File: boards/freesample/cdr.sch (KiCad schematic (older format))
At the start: 75 parts, among them J6 XILINX_JTAG, U13 SIP32408, U5 TLK10232, U6 LMK61PD0A2

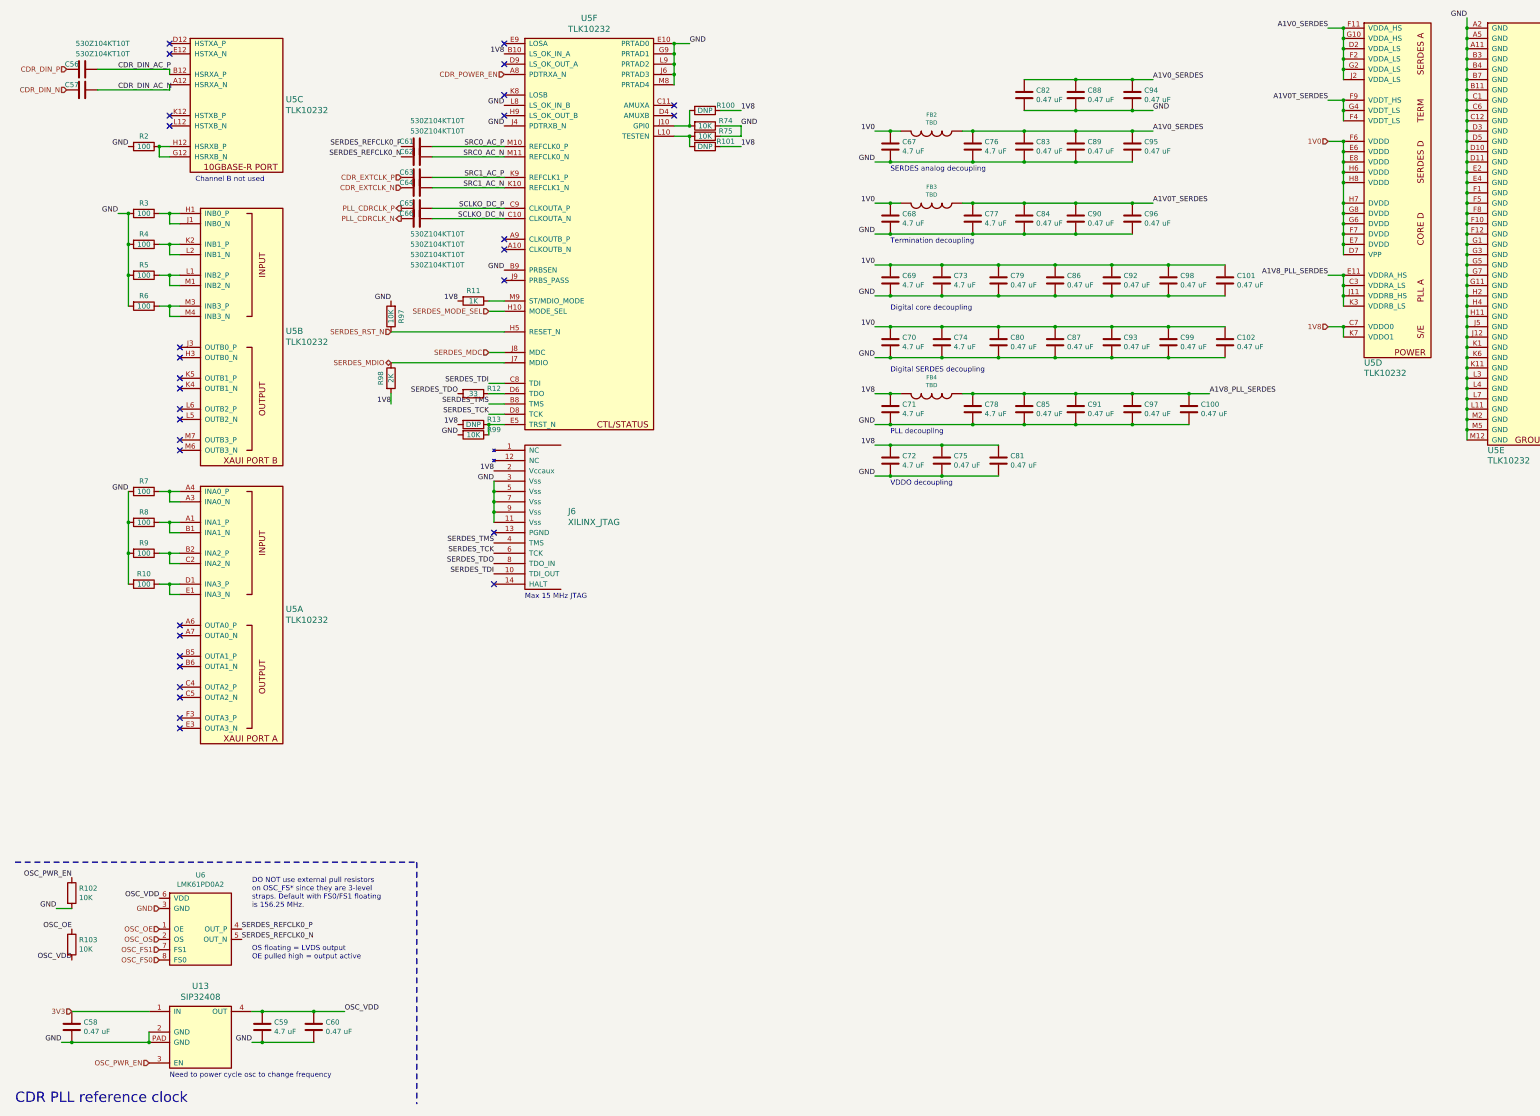
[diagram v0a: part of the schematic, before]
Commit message: Added more test points. Started picking packages for passives. Continued schematic review.
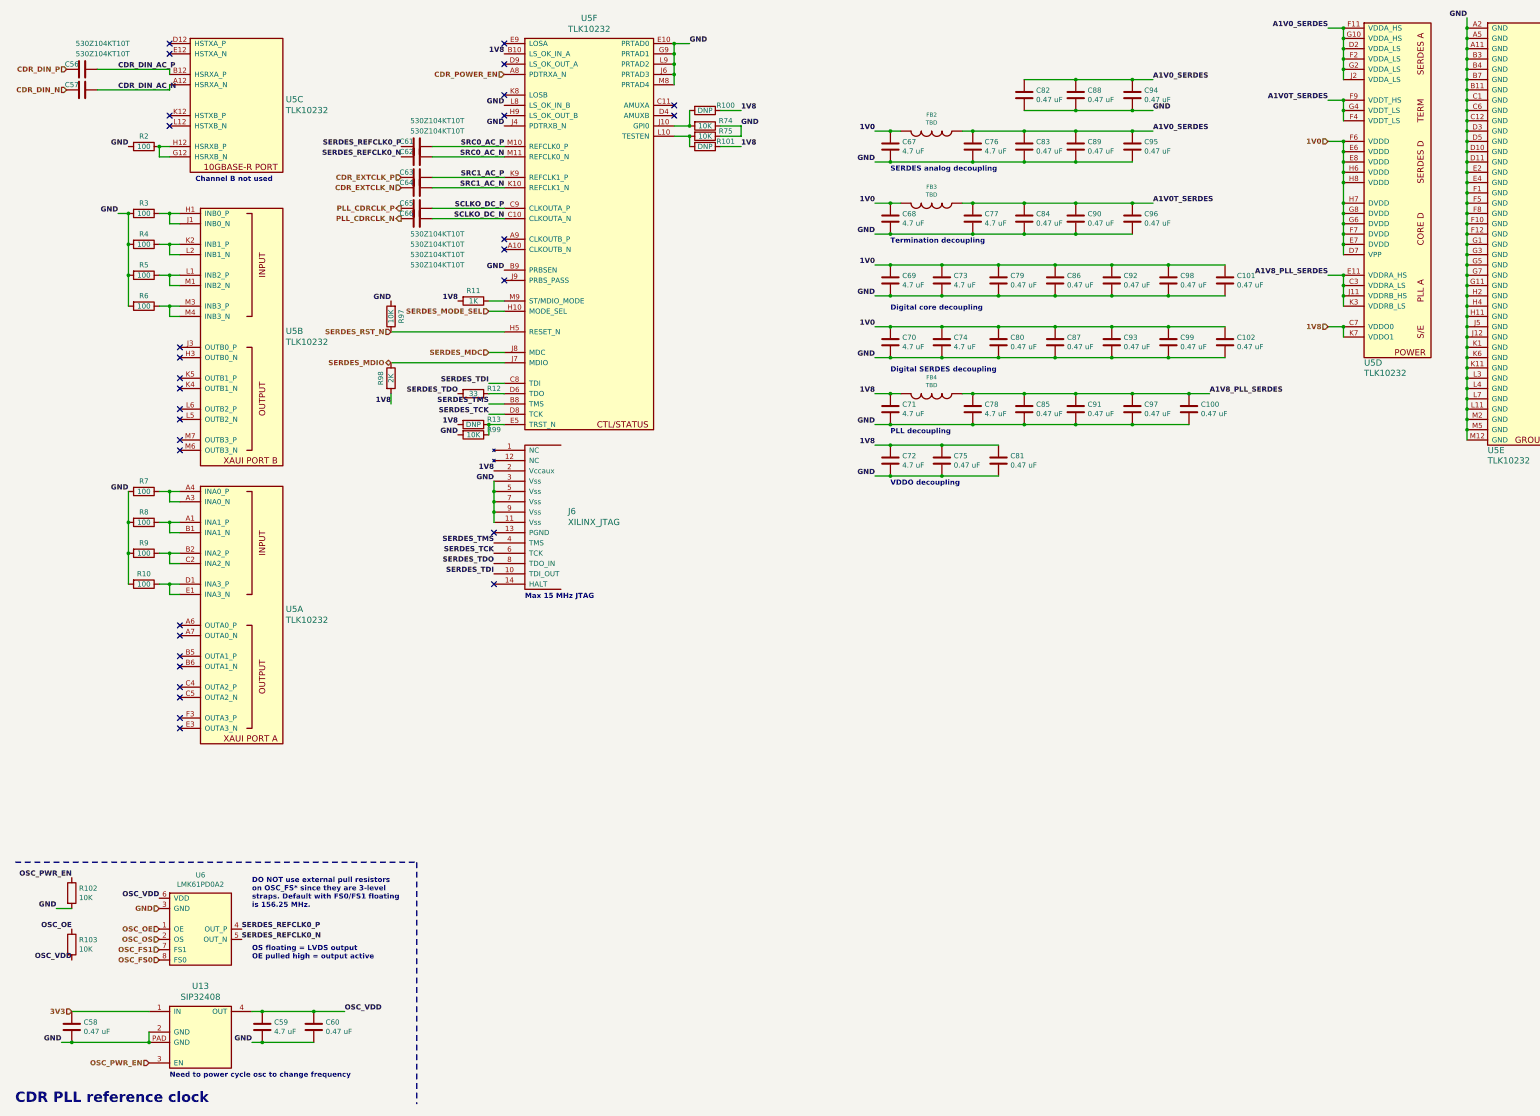
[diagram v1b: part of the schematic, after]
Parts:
- C100, C101, C102, C58, C60, C75, C79, C80, C81, C82, C83, C84, C85, C86, C87, C88, C89, C90, C91, C92, C93, C94, C95, C96, C97, C98, C99: footprint (none) -> azonenberg_pcb:EIA_0402_CAP_NOSILK
- C56, C57, C61, C62, C63, C64, C65, C66: footprint (none) -> azonenberg_pcb:EIA_0201_CAP_NOSILK
- C59, C67, C68, C69, C70, C71, C72, C73, C74, C76, C77, C78: footprint (none) -> azonenberg_pcb:EIA_0603_CAP_NOSILK
- J6: footprint (none) -> azonenberg_pcb:XILINX_JTAG_PTH_MOLEX_0878311420
- R10, R102, R103, R11, R12, R13, R2, R3, R4, R5, R6, R7, R74, R75, R8, R9, R97, R99: footprint (none) -> azonenberg_pcb:EIA_0402_RES_NOSILK
- U5: footprint (none) -> azonenberg_pcb:BGA_144_13x13_FULLARRAY_1MM

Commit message: Continued assigning footprints
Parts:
- FB2, FB3: value TBD -> BLM31KN121SZ1L; footprint (none) -> azonenberg_pcb:EIA_1206_CAP_NOSILK
- FB4: value TBD -> BLM15PX121SN1D; footprint (none) -> azonenberg_pcb:EIA_0402_CAP_NOSILK
- R100, R101, R98: footprint (none) -> azonenberg_pcb:EIA_0402_RES_NOSILK
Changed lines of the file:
@@
 Sheet 4 12
 Title "FREESAMPLE Oscilloscope"
-Date "2019-03-15"
+Date "2019-03-16"
 Rev "0.1"
 Comp "Andrew D. Zonenberg / Antikernel Labs"
@@
 P 9450 4250
 F 0 "FB4" V 9292 4250 40  0000 C CNN
-F 1 "TBD" V 9368 4250 40  0000 C CNN
-F 2 "" H 9450 4250 60  0001 C CNN
+F 1 "BLM15PX121SN1D" V 9368 4250 40  0000 C CNN
+F 2 "azonenberg_pcb:EIA_0402_CAP_NOSILK" H 9450 4250 60  0001 C CNN
 F 3 "" H 9450 4250 60  0000 C CNN
 	1    9450 4250
@@
 P 9450 2400
 F 0 "FB3" V 9292 2400 40  0000 C CNN
-F 1 "TBD" V 9368 2400 40  0000 C CNN
-F 2 "" H 9450 2400 60  0001 C CNN
+F 1 "BLM31KN121SZ1L" V 9368 2400 40  0000 C CNN
+F 2 "azonenberg_pcb:EIA_1206_CAP_NOSILK" H 9450 2400 60  0001 C CNN
 F 3 "" H 9450 2400 60  0000 C CNN
 	1    9450 2400
@@
 P 9450 1700
 F 0 "FB2" V 9292 1700 40  0000 C CNN
-F 1 "TBD" V 9368 1700 40  0000 C CNN
-F 2 "" H 9450 1700 60  0001 C CNN
+F 1 "BLM31KN121SZ1L" V 9368 1700 40  0000 C CNN
+F 2 "azonenberg_pcb:EIA_1206_CAP_NOSILK" H 9450 1700 60  0001 C CNN
 F 3 "" H 9450 1700 60  0000 C CNN
 	1    9450 1700
@@
 F 0 "R98" V 4100 4100 50  0000 C CNN
 F 1 "2K" V 4200 4100 50  0000 C CNN
-F 2 "" V 4130 4100 50  0001 C CNN
+F 2 "azonenberg_pcb:EIA_0402_RES_NOSILK" V 4130 4100 50  0001 C CNN
 F 3 "" H 4200 4100 50  0001 C CNN
 	1    4200 4100
@@
 F 0 "R101" V 7200 2050 50  0000 C CNN
 F 1 "DNP" V 7250 1850 50  0000 C CNN
-F 2 "" V 7180 1850 50  0001 C CNN
+F 2 "azonenberg_pcb:EIA_0402_RES_NOSILK" V 7180 1850 50  0001 C CNN
 F 3 "" H 7250 1850 50  0001 C CNN
 	1    7250 1850
@@
 F 0 "R100" V 7200 1700 50  0000 C CNN
 F 1 "DNP" V 7250 1500 50  0000 C CNN
-F 2 "" V 7180 1500 50  0001 C CNN
+F 2 "azonenberg_pcb:EIA_0402_RES_NOSILK" V 7180 1500 50  0001 C CNN
 F 3 "" H 7250 1500 50  0001 C CNN
 	1    7250 1500

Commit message: Continued selecting component footprints and working on schematic review
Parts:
- U13: footprint (none) -> azonenberg_pcb:DFN_4_0.5MM_1.6x1.2MM
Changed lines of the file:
@@
 F 0 "U13" H 2350 11597 60  0000 C CNN
 F 1 "SIP32408" H 2350 11491 60  0000 C CNN
-F 2 "" H 2050 10800 60  0001 C CNN
+F 2 "azonenberg_pcb:DFN_4_0.5MM_1.6x1.2MM" H 2050 10800 60  0001 C CNN
 F 3 "" H 2050 10800 60  0000 C CNN
 	1    2050 10800

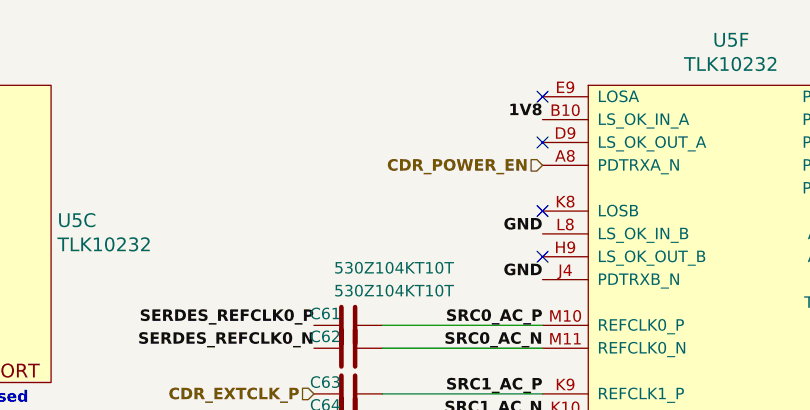
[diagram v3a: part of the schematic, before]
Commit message: Continued design review. Changed termination on DFFs to 1V8. Added some pull resistors to keep DFFs in reset during boot.
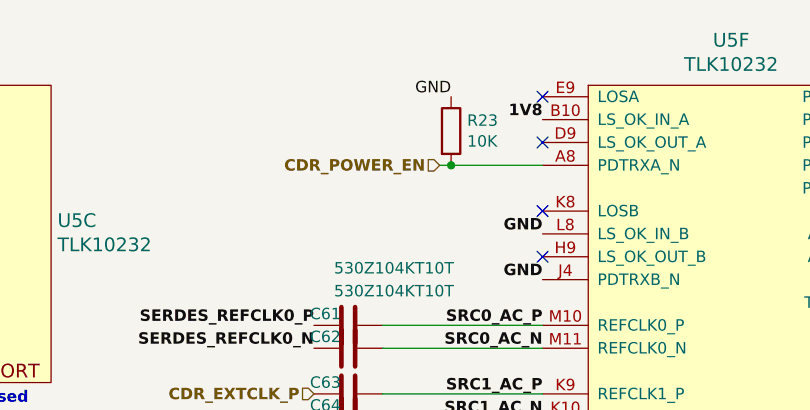
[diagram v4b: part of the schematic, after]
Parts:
- added R23: 10K, azonenberg_pcb:EIA_0402_RES_NOSILK, symbol device:R
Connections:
- net CDR_POWER_EN: now also R23.2
- net GND: now also R23.1
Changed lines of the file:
@@
 Sheet 4 12
 Title "FREESAMPLE Oscilloscope"
-Date "2019-03-16"
+Date "2019-03-17"
 Rev "0.1"
 Comp "Andrew D. Zonenberg / Antikernel Labs"
@@
 Text Notes 550  11150 0    100  ~ 6
 CDR PLL reference clock
-Text HLabel 5300 1150 0    50   Input ~ 6
+Text HLabel 4850 1150 0    50   Input ~ 6
 CDR_POWER_EN
 NoConn ~ 6950 1550
@@
 Text Label 1100 9450 2    50   ~ 6
 OSC_OE
+Wire Wire Line
+	4850 1150 4900 1150
+$Comp
+L device:R R23
+U 1 1 5D06136A
+P 4900 1000
+F 0 "R23" H 4970 1046 50  0000 L CNN
+F 1 "10K" H 4970 955 50  0000 L CNN
+F 2 "azonenberg_pcb:EIA_0402_RES_NOSILK" V 4830 1000 50  0001 C CNN
+F 3 "" H 4900 1000 50  0001 C CNN
+	1    4900 1000
+	1    0    0    -1
+$EndComp
+Connection ~ 4900 1150
+Wire Wire Line
+	4900 1150 5300 1150
+Text Label 4900 850  2    50   ~ 0
+GND
 $EndSCHEMATC

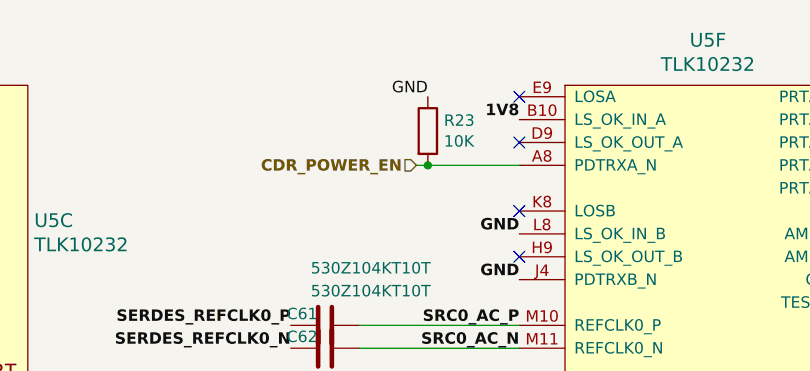
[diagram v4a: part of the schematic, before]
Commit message: Added fiducials
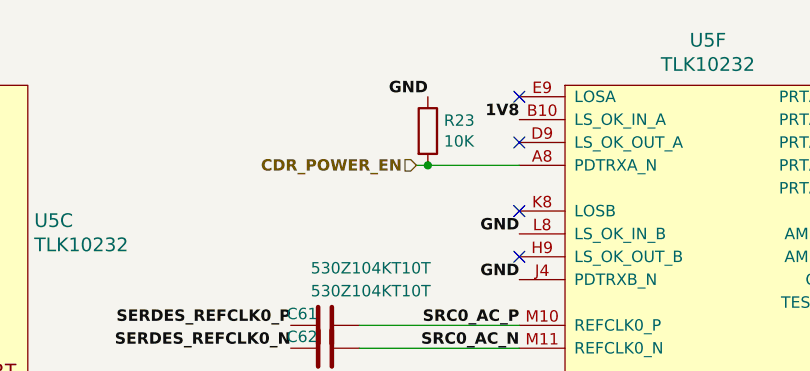
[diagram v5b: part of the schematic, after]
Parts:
- U6: footprint (none) -> azonenberg_pcb:QFN_8_5x7MM_TI_SIA
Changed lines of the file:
@@
 F 0 "U6" H 2350 10675 50  0000 C CNN
 F 1 "LMK61PD0A2" H 2350 10584 50  0000 C CNN
-F 2 "" H 2300 9750 50  0001 C CNN
+F 2 "azonenberg_pcb:QFN_8_5x7MM_TI_SIA" H 2300 9750 50  0001 C CNN
 F 3 "" H 2300 9750 50  0001 C CNN
 	1    2050 9800
@@
 Wire Wire Line
 	4900 1150 5300 1150
-Text Label 4900 850  2    50   ~ 0
+Text Label 4900 850  2    50   ~ 6
 GND
 $EndSCHEMATC

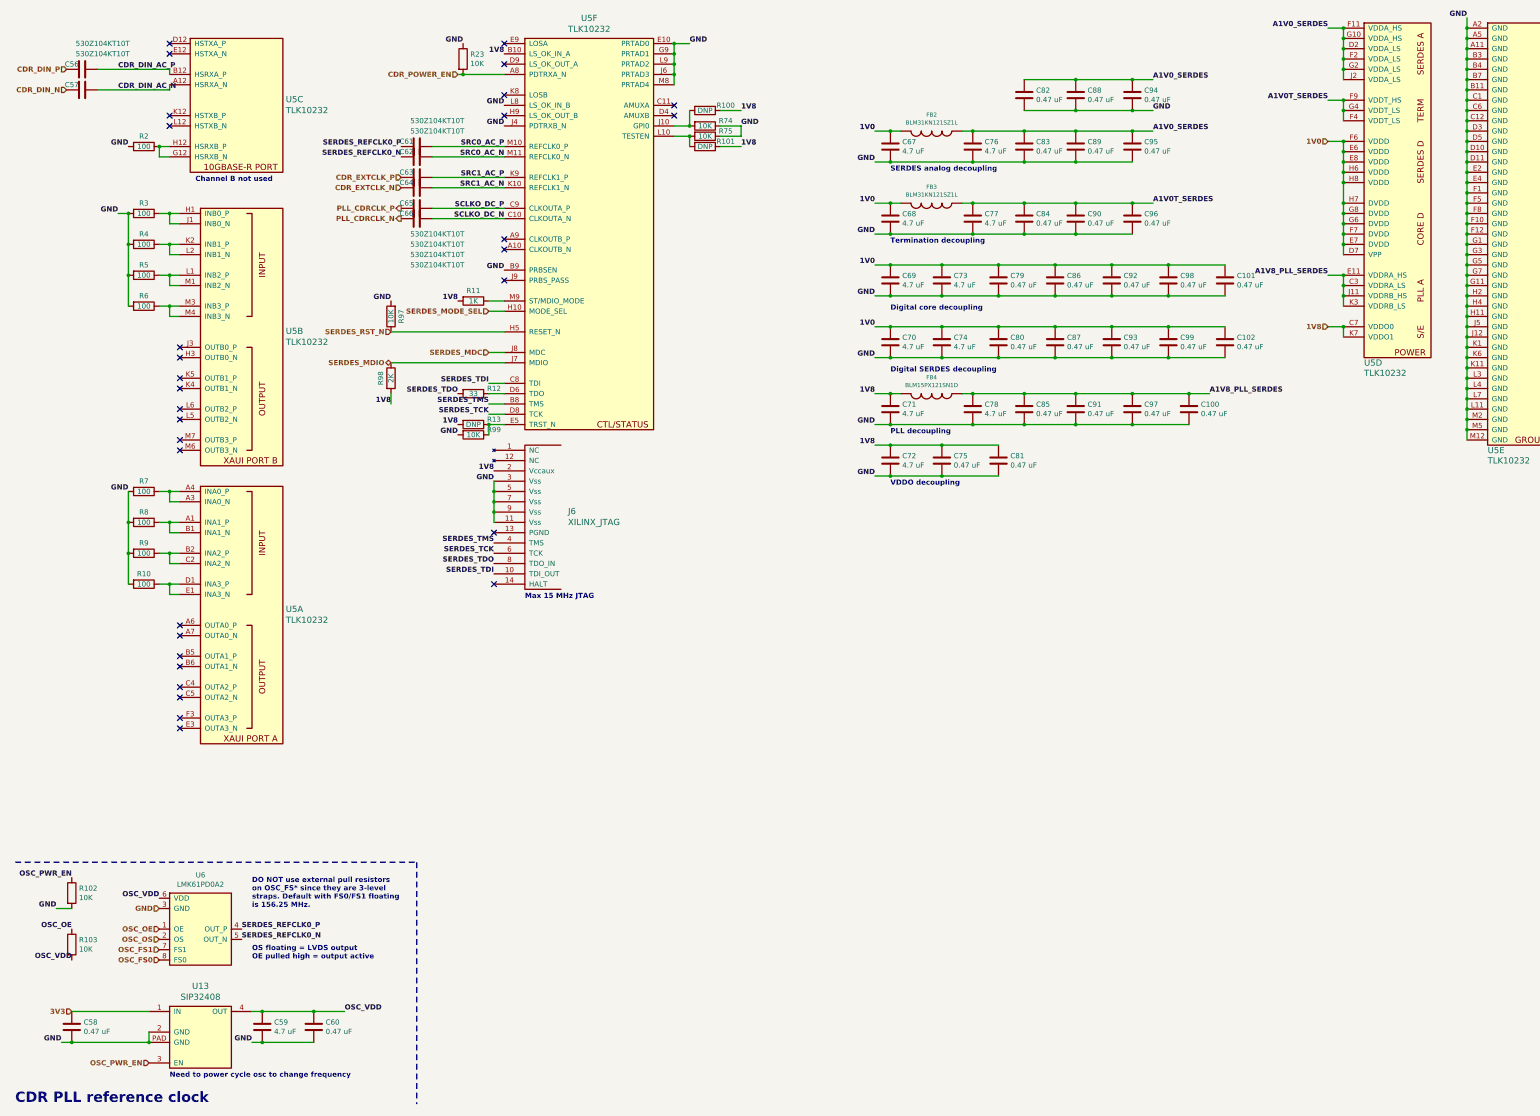
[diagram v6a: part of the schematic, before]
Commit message: Began layout on clock recovery block
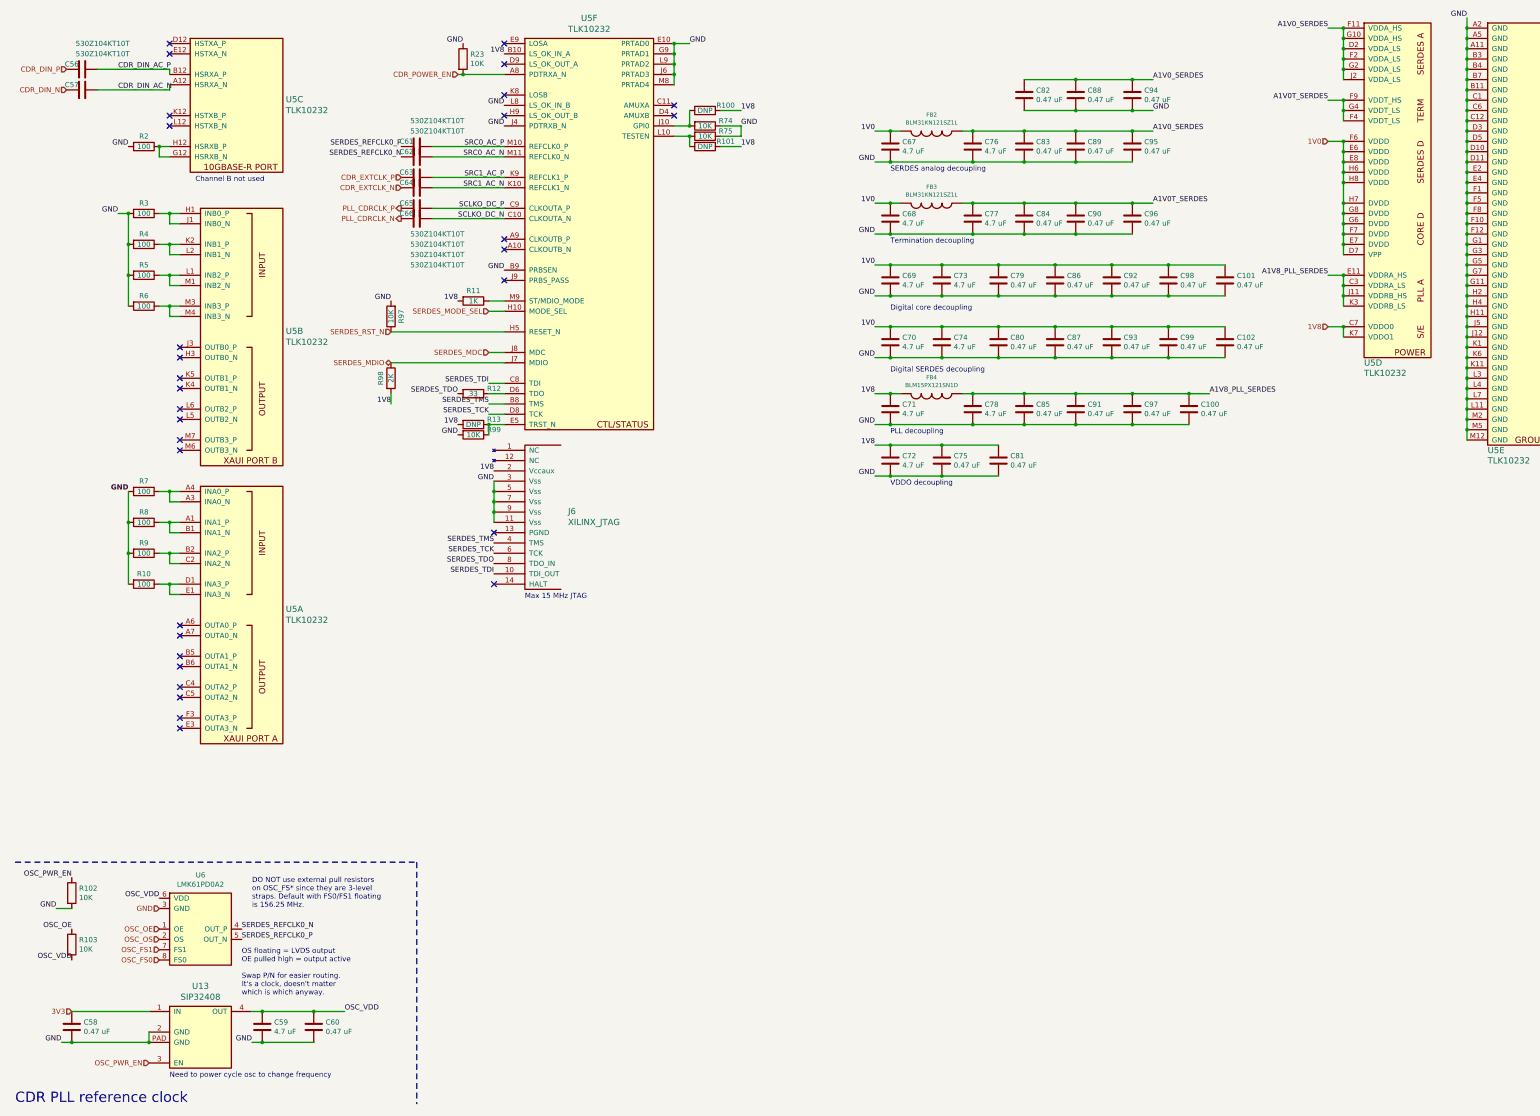
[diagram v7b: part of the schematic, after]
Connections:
- net SERDES_REFCLK0_N: now also U6.4 (OUT_P); no longer U6.5 (OUT_N)
- net SERDES_REFCLK0_P: now also U6.5 (OUT_N); no longer U6.4 (OUT_P)
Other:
- note added: "OS floating = LVDS output\nOE pulled high = output active\n\nSwap P/N for easier routing.\nIt's a clock, doesn't matter\nwhich is which anyway."
- note removed: "OS floating = LVDS output\nOE pulled high = output active"

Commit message: Finished initial layout of CDR subsystem
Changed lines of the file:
@@
 Wire Wire Line
 	1650 5800 1650 5500
-Text Label 1650 5200 2    50   ~ 10
+Text Label 1650 5200 2    50   ~ 0
 GND
 NoConn ~ 2150 6500
